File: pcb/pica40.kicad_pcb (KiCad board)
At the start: 2 copper layers, 135 x 93.7 mm, 63 parts, among them SW1 SW_PUSH, SW10 SW_PUSH, SW11 SW_PUSH, SW12 SW_PUSH, SW13 SW_PUSH, SW14 SW_PUSH, SW15 SW_PUSH, SW16 SW_PUSH, SW17 SW_PUSH, SW18 SW_PUSH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

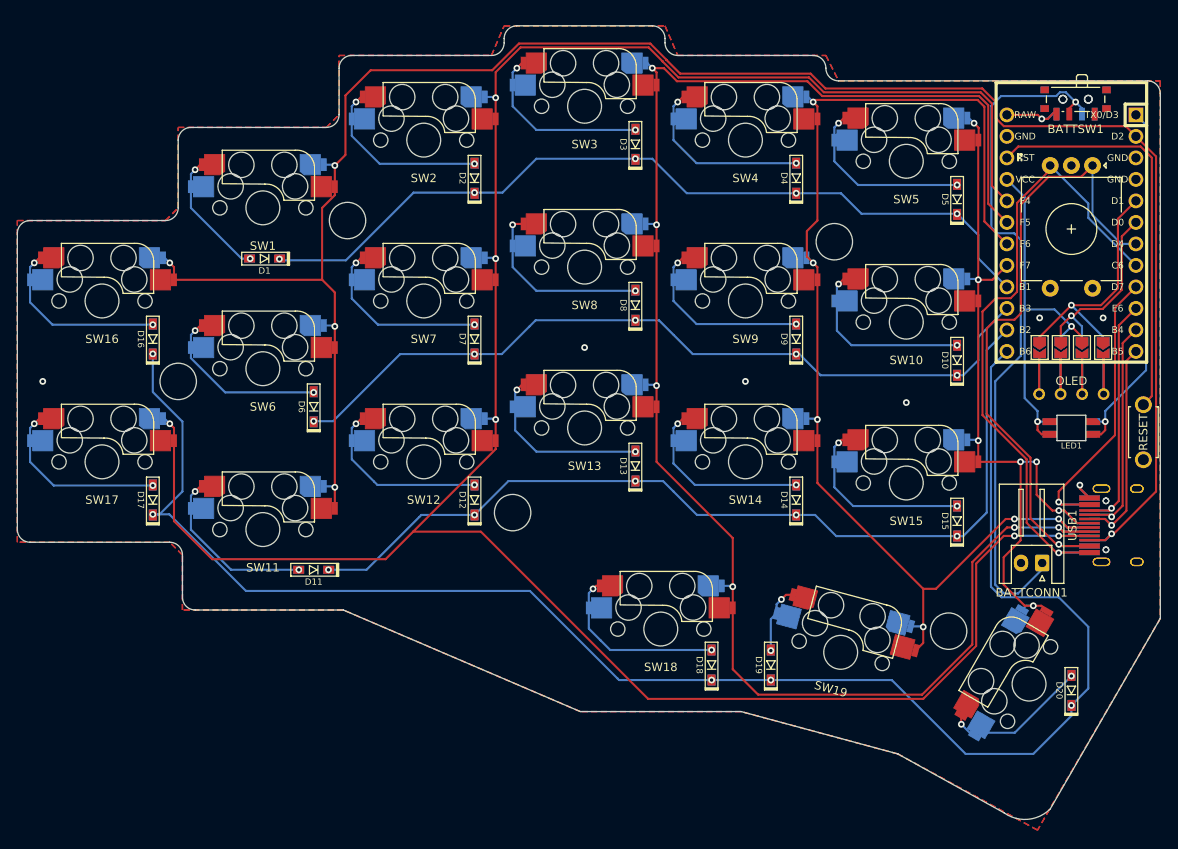
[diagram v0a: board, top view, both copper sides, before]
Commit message: flip oled jumpers
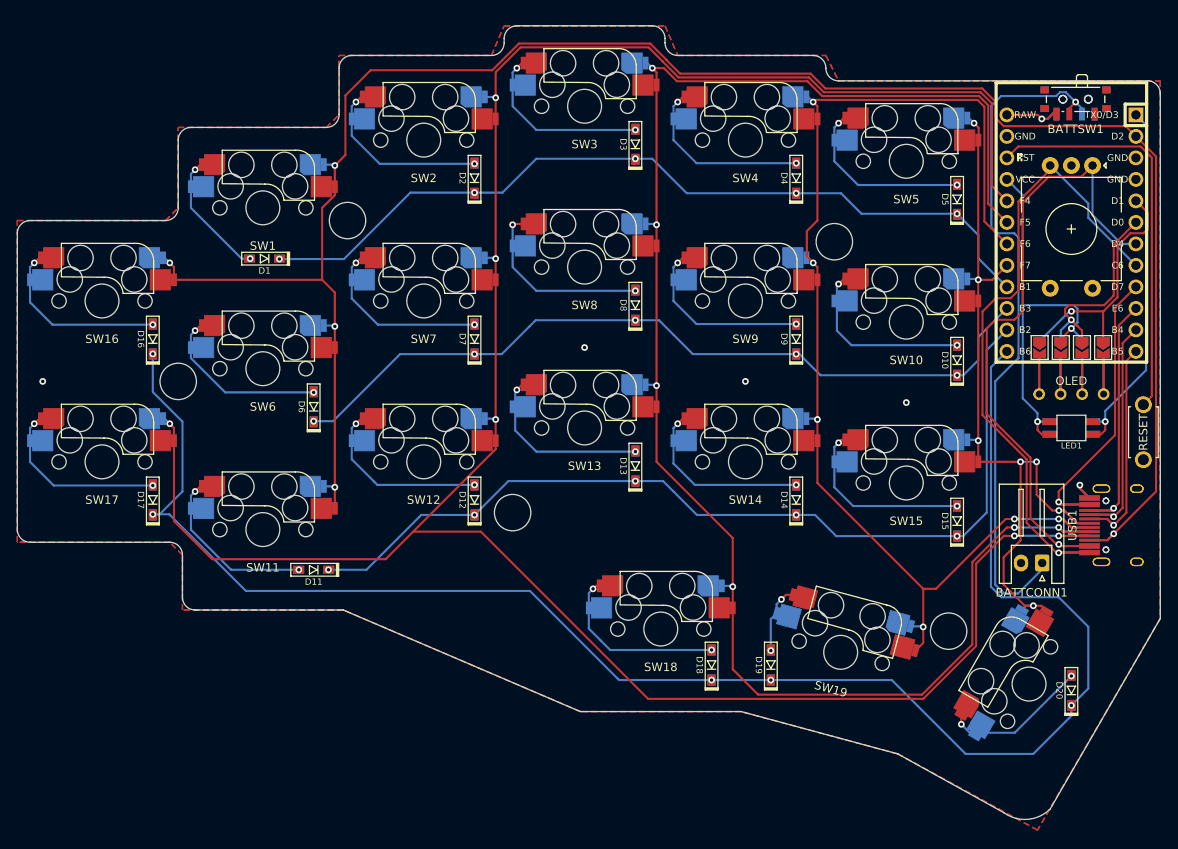
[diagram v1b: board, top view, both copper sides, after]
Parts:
- JP1, JP3, JP5, JP7: moved to B.Cu
- JP2, JP4, JP6, JP8: moved to F.Cu
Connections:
- USB1 pad 13: unconnected-(USB1-Pad13) -> (no net)
- USB2 pad 13: unconnected-(USB2-Pad13) -> (no net)
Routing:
- net VCC: track 46.2 -> 47.6 mm
- net SCL: track 23.0 -> 23.9 mm
- net Net-(D9-Pad2): track 21.7 -> 21.2 mm
- net Net-(D14-Pad2): track 21.8 -> 21.3 mm
- net Net-(D10-Pad2): track 21.8 -> 21.3 mm
- net GND: track 3.99 -> 4.01 mm, vias 7 -> 5

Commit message: logos and jlcpcb texts
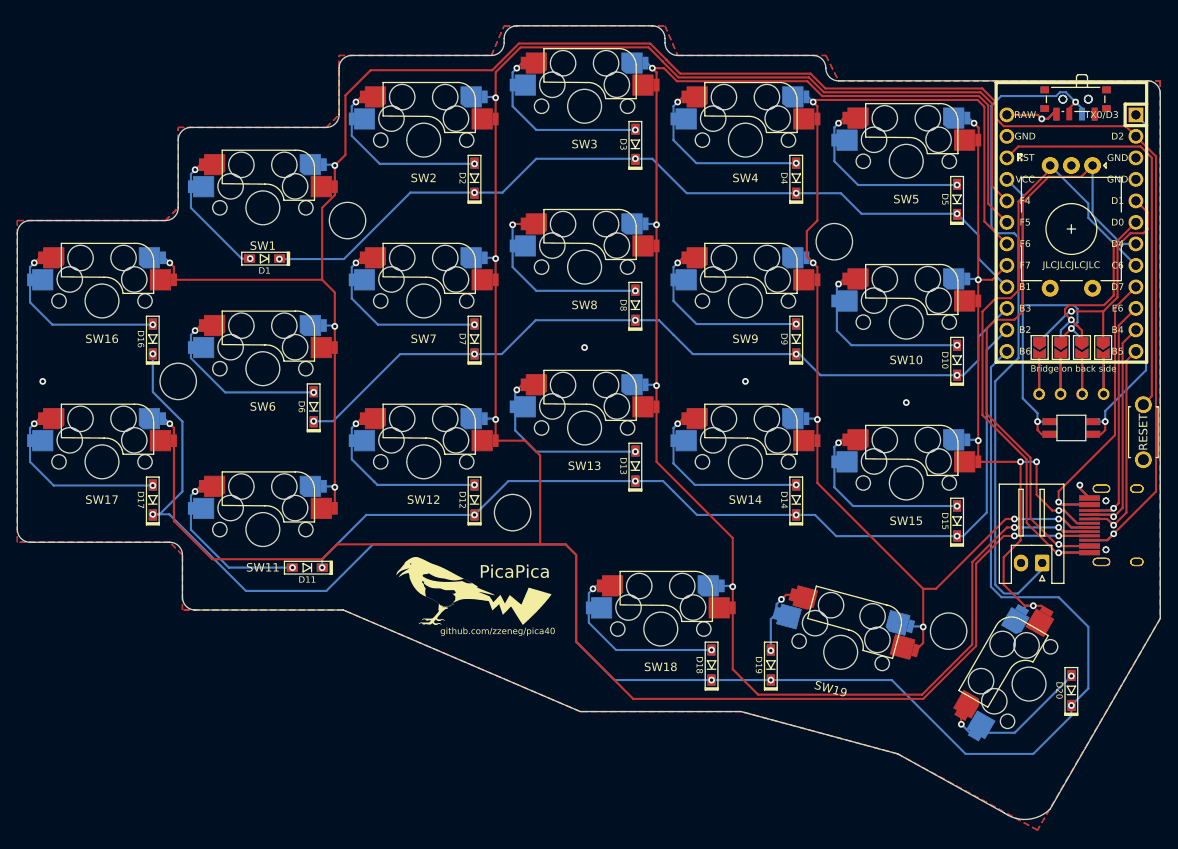
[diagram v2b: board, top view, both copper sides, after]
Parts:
- added G***: LOGO, pica:logo, F.Cu at (121.2, 118.2)
- added G***: LOGO, pica:logo_mirror, B.Cu at (121.2, 118.2)
- moved D11 0.79 mm to (102.8, 115.5)
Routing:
- net row3: track 197.8 -> 208.3 mm
- net col1: track 286.8 -> 293.2 mm
- net row2: track 108.5 -> 109.7 mm
- net Net-(D11-Pad2): track 20.5 -> 19.6 mm
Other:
- board text added: "Bridge on back side"
- board text added: "JLCJLCJLCJLC"
- board text added: "PicaPica"
- board text added: "github.com/zzeneg/pica40"

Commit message: add breakaway plate, replace battery connector
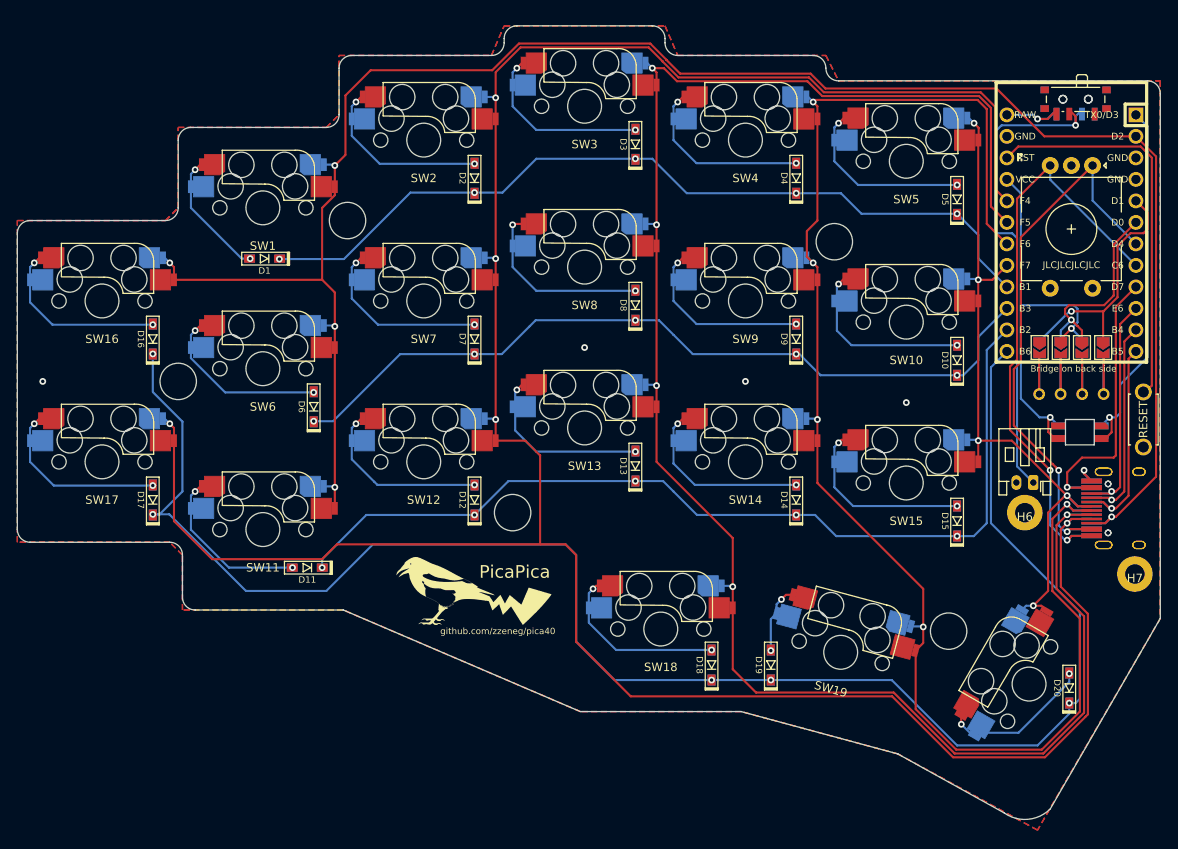
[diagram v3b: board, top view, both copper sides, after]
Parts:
- added H6: MountingHole, kbd:M2_Hole_TH, F.Cu at (187.5, 109.0)
- added H7: MountingHole, kbd:M2_Hole_TH, F.Cu at (200.5, 116.2)
- BATTCONN1: footprint Connector_JST:JST_XH_S2B-XH-A_1x02_P2.50mm_Horizontal -> pica:JST_PH_S2B-PH-K_1x02_P2.00mm_Horizontal
- moved BATTCONN1 9.56 mm to (188.5, 105.5)
- moved USB1 2.02 mm to (203.6, 108.5)
- moved USB2 2.02 mm to (203.6, 108.5)
- moved RESET1 1.50 mm to (201.5, 98.0)
- moved LED1 1.12 mm to (194.0, 99.5)
- moved D20 0.37 mm to (192.8, 129.7)
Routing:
- net col3: track 141.4 -> 177.0 mm, vias 6 -> 5
- net BATT: track 81.5 -> 58.4 mm
- net col1: track 293.2 -> 311.1 mm, vias 6 -> 5
- net col2: track 197.7 -> 215.1 mm, vias 6 -> 5
- net ENCA: track 77.0 -> 67.3 mm, vias 1 -> 2
- net col4: track 93.5 -> 85.8 mm, vias 7 -> 5
- net ENCB: track 77.5 -> 71.3 mm, vias 1 -> 2
- net row3: track 208.3 -> 202.9 mm
- net col0: track 233.2 -> 229.3 mm
- net row4: track 27.9 -> 24.3 mm
- net row5: track 29.1 -> 26.7 mm
- net row6: track 30.6 -> 28.3 mm
- net row7: track 36.7 -> 35.0 mm
- net VCC: track 47.6 -> 49.0 mm
- net RESET: track 47.8 -> 46.6 mm
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
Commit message: move diodes
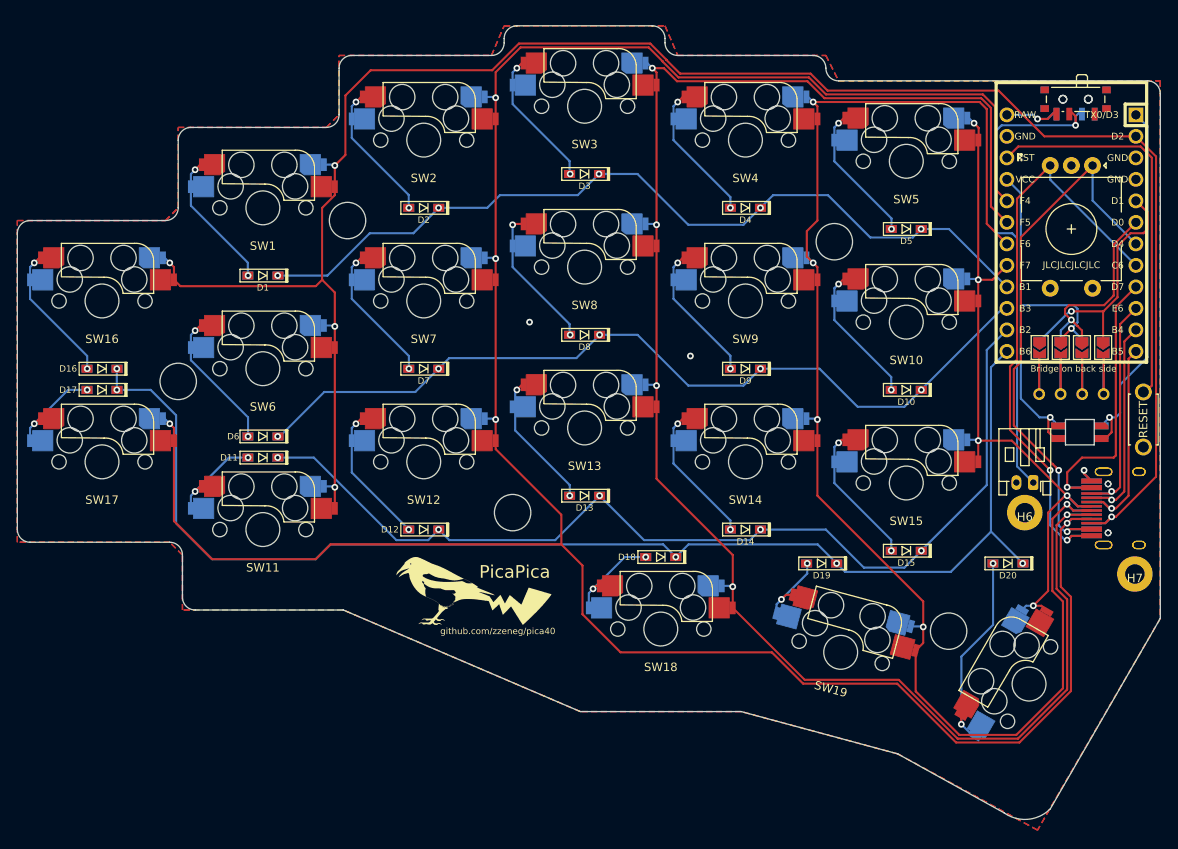
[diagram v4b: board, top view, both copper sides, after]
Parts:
- moved D20 16.4 mm to (185.5, 115.0), turned to 180 degrees
- moved D17 14.3 mm to (78.5, 94.5), turned to 180 degrees
- moved D18 14.1 mm to (144.5, 114.2), turned to 180 degrees
- moved D11 14.0 mm to (97.5, 102.5)
- moved D19 13.4 mm to (163.5, 115.0), turned to 180 degrees
- moved D10 6.95 mm to (173.5, 94.5), turned to 180 degrees
- moved D12 6.95 mm to (116.5, 111.0), turned to 180 degrees
- moved D13 6.95 mm to (135.5, 107.0), turned to 180 degrees
- moved D14 6.95 mm to (154.5, 111.0), turned to 180 degrees
- moved D15 6.95 mm to (173.5, 113.5), turned to 180 degrees
- moved D16 6.95 mm to (78.5, 92.0), turned to 180 degrees
- moved D2 6.95 mm to (116.5, 73.0), turned to 180 degrees
- moved D3 6.95 mm to (135.5, 69.0), turned to 180 degrees
- moved D4 6.95 mm to (154.5, 73.0), turned to 180 degrees
- moved D5 6.95 mm to (173.5, 75.5), turned to 180 degrees
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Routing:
- net row3: track 202.9 -> 154.2 mm
- net Net-(D17-Pad2): track 21.4 -> 11.2 mm
- net col2: track 215.1 -> 204.9 mm
- net Net-(D18-Pad2): track 21.3 -> 11.5 mm
- net col1: track 311.1 -> 301.5 mm
- net Net-(D11-Pad2): track 19.6 -> 11.1 mm
- net row2: track 110.5 -> 118.9 mm
- net col3: track 177.0 -> 169.7 mm
- net row1: track 94.4 -> 101.1 mm
- net Net-(D20-Pad2): track 18.0 -> 23.7 mm
- net Net-(D15-Pad2): track 22.1 -> 17.0 mm
- net Net-(D10-Pad2): track 21.3 -> 16.3 mm
- net Net-(D14-Pad2): track 21.3 -> 16.3 mm
- net Net-(D16-Pad2): track 21.5 -> 16.6 mm
- net Net-(D8-Pad2): track 22.0 -> 17.1 mm
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
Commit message: update and reroute
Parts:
- moved LED1 4.10 mm to (194.0, 95.4)
- moved OLED1 3.20 mm to (193.0, 91.8)
- moved U1 3.20 mm to (193.0, 72.8)
- moved BATTSW1 3.16 mm to (193.0, 57.4)
- moved BATTSW2 3.16 mm to (193.0, 57.4)
- moved RESET1 3.04 mm to (201.0, 95.0)
- moved USB1 2.93 mm to (203.6, 105.6)
- moved USB2 2.93 mm to (203.6, 105.6)
- moved D20 2.22 mm to (187.7, 115.3), turned to -90 degrees
- moved H7 2.14 mm to (199.9, 114.2)
- moved BATTCONN1 2.02 mm to (188.0, 103.5)
- moved JP1 2.00 mm to (189.2, 87.5)
- moved JP2 2.00 mm to (189.2, 87.5)
- moved JP3 2.00 mm to (191.8, 87.5)
- moved JP4 2.00 mm to (191.8, 87.5)
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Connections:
- U1 pad 10: row6 -> col3
- U1 pad 11: row5 -> col2
- U1 pad 12: row4 -> col1
- U1 pad 17: col4 -> row4
- U1 pad 18: col3 -> row5
- U1 pad 19: col2 -> row6
- U1 pad 20: col1 -> row7
- U1 pad 9: row7 -> col4
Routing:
- net col0: track 229.9 -> 349.5 mm
- net col1: track 301.5 -> 255.3 mm
- net col4: track 85.8 -> 119.2 mm
- net col2: track 204.9 -> 180.1 mm
- net row4: track 24.3 -> 38.2 mm
- net row5: track 26.7 -> 40.1 mm
- net ENCB: track 71.3 -> 58.4 mm, vias 2 -> 1
- net row6: track 28.3 -> 40.4 mm
- net col3: track 169.7 -> 160.8 mm
- net RESET: track 46.6 -> 54.3 mm
- net row7: track 35.0 -> 42.2 mm
- net row3: track 154.2 -> 159.9 mm
- net row2: track 118.9 -> 124.5 mm
- net ENCA: track 67.3 -> 62.5 mm, vias 2 -> 1
- net BATT: track 58.4 -> 54.7 mm
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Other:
- board size 135 x 93.7 mm -> 135 x 95.7 mm
